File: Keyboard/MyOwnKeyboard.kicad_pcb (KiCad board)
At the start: 2 copper layers, 465 parts, among them J1 Mini-DIN-6, Q1 RFD14N05L, SW1 SW_SPST, SW10 SW_SPST, SW100 SW_SPST, SW101 SW_SPST, SW102 SW_SPST, SW103 SW_SPST, SW104 SW_SPST, SW105 SW_SPST, SW106 SW_SPST, SW107 SW_SPST, SW108 SW_SPST, SW109 SW_SPST, SW11 SW_SPST, SW110 SW_SPST, SW111 SW_SPST, SW112 SW_SPST, SW113 SW_SPST, SW114 SW_SPST, SW12 SW_SPST, SW13 SW_SPST, SW14 SW_SPST, SW15 SW_SPST, SW16 SW_SPST, SW17 SW_SPST, SW18 SW_SPST, SW19 SW_SPST, SW2 SW_SPST, SW20 SW_SPST, SW21 SW_SPST, SW22 SW_SPST, SW23 SW_SPST, SW24 SW_SPST, SW25 SW_SPST, SW26 SW_SPST, SW27 SW_SPST, SW28 SW_SPST, SW29 SW_SPST, SW3 SW_SPST, SW30 SW_SPST, SW31 SW_SPST, SW32 SW_SPST, SW33 SW_SPST, SW34 SW_SPST, SW35 SW_SPST, SW36 SW_SPST, SW37 SW_SPST, SW38 SW_SPST, SW39 SW_SPST, SW4 SW_SPST, SW40 SW_SPST, SW41 SW_SPST, SW42 SW_SPST, SW43 SW_SPST, SW44 SW_SPST, SW45 SW_SPST, SW46 SW_SPST, SW47 SW_SPST, SW48 SW_SPST, SW49 SW_SPST, SW5 SW_SPST, SW50 SW_SPST, SW51 SW_SPST, SW52 SW_SPST, SW53 SW_SPST, SW54 SW_SPST, SW55 SW_SPST, SW56 SW_SPST, SW57 SW_SPST, SW58 SW_SPST, SW59 SW_SPST, SW6 SW_SPST, SW60 SW_SPST, SW61 SW_SPST, SW62 SW_SPST, SW63 SW_SPST, SW64 SW_SPST, SW65 SW_SPST, SW66 SW_SPST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

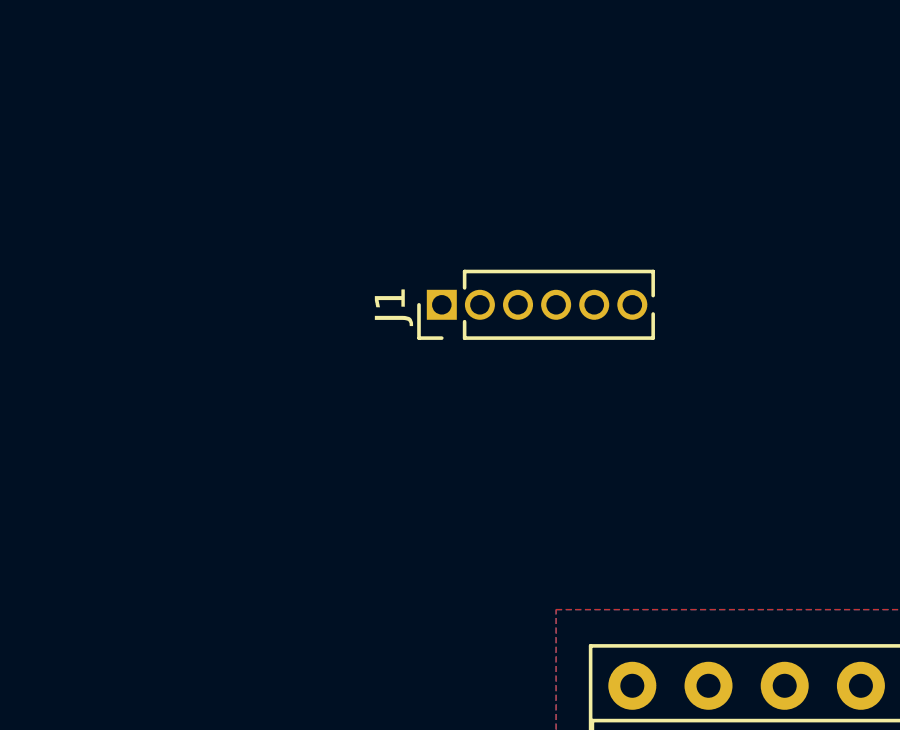
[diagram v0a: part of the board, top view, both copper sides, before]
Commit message: Update keyboard to match changes to keypad
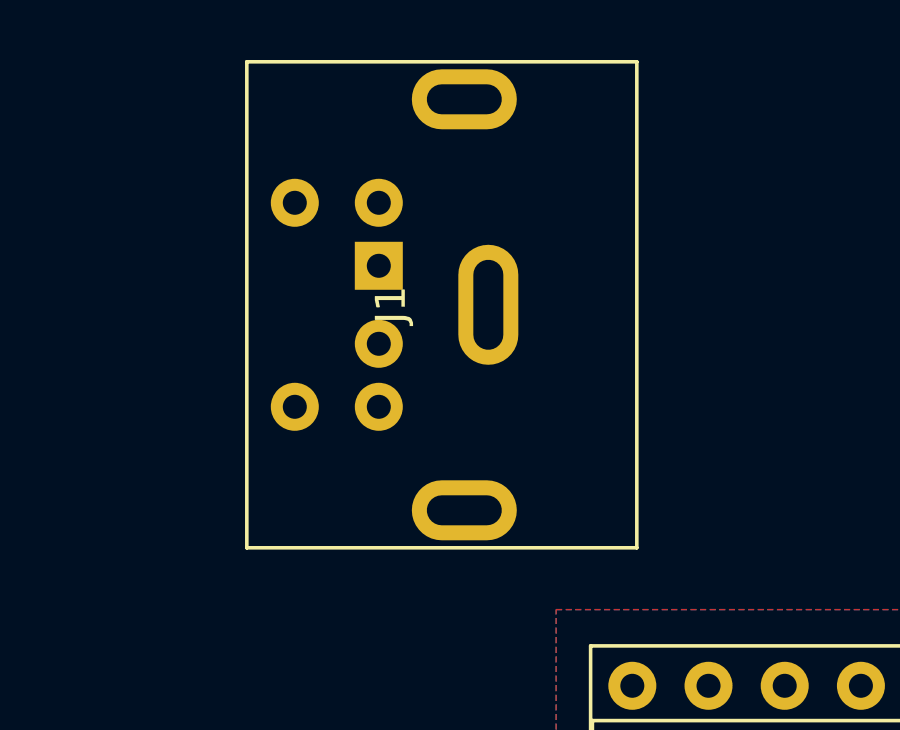
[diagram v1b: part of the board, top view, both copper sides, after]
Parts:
- J1: footprint Connector_PinHeader_1.27mm:PinHeader_1x06_P1.27mm_Vertical -> MyOwnKeyboard:Connector_Mini-DIN_Female_6Pin_2rows
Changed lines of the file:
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@@
     (add_net f)
+  )
+  (module MyOwnKeyboard:Connector_Mini-DIN_Female_6Pin_2rows (layer F.Cu)
+    (at 167.64 39.37 90)
+    (descr "A footprint for the generic 6 pin Mini-DIN through hole connector with shell.")
+    (tags "mini din 6pin connector socket")
+    (fp_text reference J1 (at 0 -1.695 90) (layer F.SilkS)
+      (effects (font (size 1 1) (thickness 0.15)))
+    )
+    (fp_text value Mini-DIN-6 (at 0 8.045 90) (layer F.Fab)
+      (effects (font (size 1 1) (thickness 0.15)))
+    )
+    (fp_line (start 8.49 6.9) (end -8.51 6.9) (layer F.CrtYd) (width 0.05))
+    (fp_line (start 8.49 6.9) (end 8.49 -7.15) (layer F.CrtYd) (width 0.05))
+    (fp_line (start -8.51 -7.15) (end -8.51 6.9) (layer F.CrtYd) (width 0.05))
+    (fp_line (start -8.51 -7.15) (end 8.49 -7.15) (layer F.CrtYd) (width 0.05))
+    (fp_line (start -8.1 6.5) (end 8.1 6.5) (layer F.SilkS) (width 0.12))
+    (fp_line (start -8.1 -6.5) (end 8.1 -6.5) (layer F.SilkS) (width 0.12))
+    (fp_line (start -8.1 -6.5) (end -8.1 6.5) (layer F.SilkS) (width 0.12))
+    (fp_line (start 8.1 -6.5) (end 8.1 6.5) (layer F.SilkS) (width 0.12))
+    (fp_line (start -8 -6.4) (end 8 -6.4) (layer F.Fab) (width 0.1))
+    (fp_line (start -8 6.4) (end -8 -6.4) (layer F.Fab) (width 0.1))
+    (fp_line (start 8 6.4) (end -8 6.4) (layer F.Fab) (width 0.1))
+    (fp_line (start 8 -6.4) (end 8 6.4) (layer F.Fab) (width 0.1))
+    (fp_text user %R (at 0 3.175) (layer F.Fab)
+      (effects (font (size 1 1) (thickness 0.15)))
+    )
+    (pad 7 thru_hole oval (at 0 1.55 90) (size 4 2) (drill oval 3 1) (layers *.Cu *.Mask))
+    (pad 6 thru_hole circle (at -3.4 -4.9 90) (size 1.6 1.6) (drill 0.8) (layers *.Cu *.Mask)
+      (net 268 "Net-(J1-Pad6)"))
+    (pad 5 thru_hole circle (at 3.4 -4.9 90) (size 1.6 1.6) (drill 0.8) (layers *.Cu *.Mask)
+      (net 153 /Clk))
+    (pad 4 thru_hole circle (at -3.4 -2.1 90) (size 1.6 1.6) (drill 0.8) (layers *.Cu *.Mask)
+      (net 141 5v))
+    (pad 3 thru_hole circle (at 3.4 -2.1 90) (size 1.6 1.6) (drill 0.8) (layers *.Cu *.Mask)
+      (net 269 GND))
+    (pad 2 thru_hole circle (at -1.3 -2.1 90) (size 1.6 1.6) (drill 0.8) (layers *.Cu *.Mask)
+      (net 270 "Net-(J1-Pad2)"))
+    (pad 1 thru_hole rect (at 1.3 -2.1 90) (size 1.6 1.6) (drill 0.8) (layers *.Cu *.Mask)
+      (net 151 /Data))
+    (pad 7 thru_hole oval (at 6.85 0.75 90) (size 2 3.5) (drill oval 1 2.5) (layers *.Cu *.Mask))
+    (pad 7 thru_hole oval (at -6.85 0.75 90) (size 2 3.5) (drill oval 1 2.5) (layers *.Cu *.Mask))
   )
   (module Package_DIP:DIP-40_W15.24mm_Socket (layer F.Cu)
@@
       (at (xyz 0 0 0))
       (scale (xyz 1 1 1))
-      (rotate (xyz 0 0 0))
-    )
-  )
-  (module Connector_PinHeader_1.27mm:PinHeader_1x06_P1.27mm_Vertical (layer F.Cu)
-    (at 167.64 39.37 90)
-    (descr "Through hole straight pin header, 1x06, 1.27mm pitch, single row")
-    (tags "Through hole pin header THT 1x06 1.27mm single row")
-    (fp_text reference J1 (at 0 -1.695 90) (layer F.SilkS)
-      (effects (font (size 1 1) (thickness 0.15)))
-    )
-    (fp_text value Mini-DIN-6 (at 0 8.045 90) (layer F.Fab)
-      (effects (font (size 1 1) (thickness 0.15)))
-    )
-    (fp_text user %R (at 0 3.175) (layer F.Fab)
-      (effects (font (size 1 1) (thickness 0.15)))
-    )
-    (fp_line (start 1.55 -1.15) (end -1.55 -1.15) (layer F.CrtYd) (width 0.05))
-    (fp_line (start 1.55 7.5) (end 1.55 -1.15) (layer F.CrtYd) (width 0.05))
-    (fp_line (start -1.55 7.5) (end 1.55 7.5) (layer F.CrtYd) (width 0.05))
-    (fp_line (start -1.55 -1.15) (end -1.55 7.5) (layer F.CrtYd) (width 0.05))
-    (fp_line (start -1.11 -0.76) (end 0 -0.76) (layer F.SilkS) (width 0.12))
-    (fp_line (start -1.11 0) (end -1.11 -0.76) (layer F.SilkS) (width 0.12))
-    (fp_line (start 0.563471 0.76) (end 1.11 0.76) (layer F.SilkS) (width 0.12))
-    (fp_line (start -1.11 0.76) (end -0.563471 0.76) (layer F.SilkS) (width 0.12))
-    (fp_line (start 1.11 0.76) (end 1.11 7.045) (layer F.SilkS) (width 0.12))
-    (fp_line (start -1.11 0.76) (end -1.11 7.045) (layer F.SilkS) (width 0.12))
-    (fp_line (start 0.30753 7.045) (end 1.11 7.045) (layer F.SilkS) (width 0.12))
-    (fp_line (start -1.11 7.045) (end -0.30753 7.045) (layer F.SilkS) (width 0.12))
-    (fp_line (start -1.05 -0.11) (end -0.525 -0.635) (layer F.Fab) (width 0.1))
-    (fp_line (start -1.05 6.985) (end -1.05 -0.11) (layer F.Fab) (width 0.1))
-    (fp_line (start 1.05 6.985) (end -1.05 6.985) (layer F.Fab) (width 0.1))
-    (fp_line (start 1.05 -0.635) (end 1.05 6.985) (layer F.Fab) (width 0.1))
-    (fp_line (start -0.525 -0.635) (end 1.05 -0.635) (layer F.Fab) (width 0.1))
-    (pad 6 thru_hole oval (at 0 6.35 90) (size 1 1) (drill 0.65) (layers *.Cu *.Mask)
-      (net 268 "Net-(J1-Pad6)"))
-    (pad 5 thru_hole oval (at 0 5.08 90) (size 1 1) (drill 0.65) (layers *.Cu *.Mask)
-      (net 153 /Clk))
-    (pad 4 thru_hole oval (at 0 3.81 90) (size 1 1) (drill 0.65) (layers *.Cu *.Mask)
-      (net 141 5v))
-    (pad 3 thru_hole oval (at 0 2.54 90) (size 1 1) (drill 0.65) (layers *.Cu *.Mask)
-      (net 269 GND))
-    (pad 2 thru_hole oval (at 0 1.27 90) (size 1 1) (drill 0.65) (layers *.Cu *.Mask)
-      (net 270 "Net-(J1-Pad2)"))
-    (pad 1 thru_hole rect (at 0 0 90) (size 1 1) (drill 0.65) (layers *.Cu *.Mask)
-      (net 151 /Data))
-    (model ${KISYS3DMOD}/Connector_PinHeader_1.27mm.3dshapes/PinHeader_1x06_P1.27mm_Vertical.wrl
-      (at (xyz 0 0 0))
-      (scale (xyz 1 1 1))

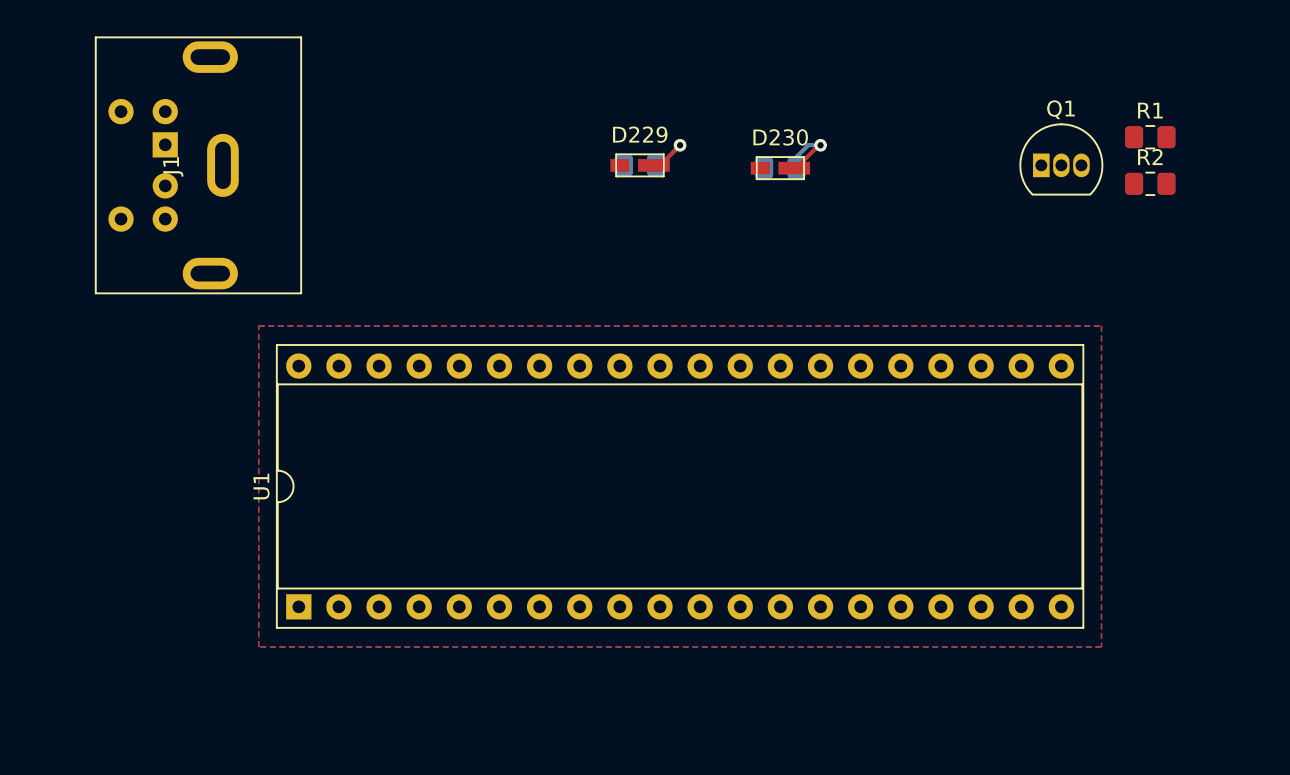
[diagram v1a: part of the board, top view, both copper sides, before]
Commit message: Update keyboard PCB template to match schematic
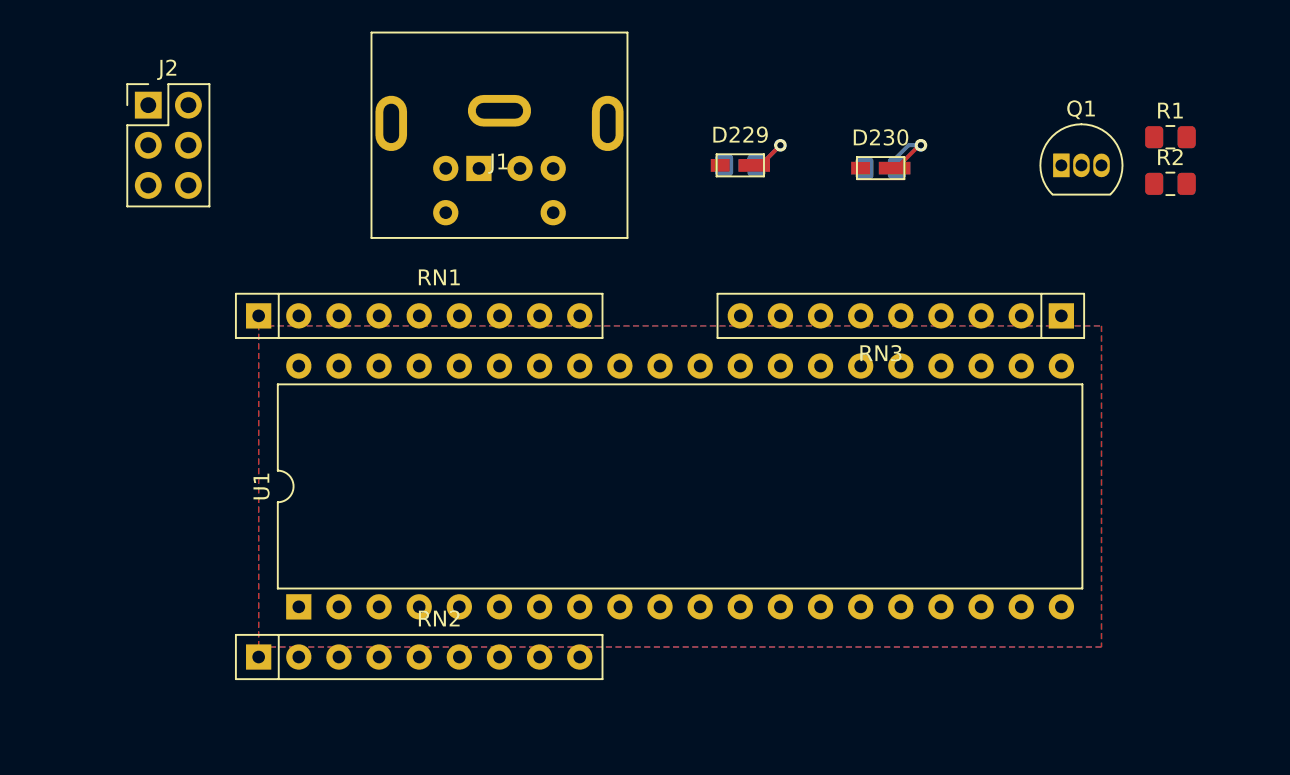
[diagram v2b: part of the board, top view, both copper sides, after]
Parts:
- added J2: ISP Header, Connector_PinHeader_2.54mm:PinHeader_2x03_P2.54mm_Vertical, F.Cu at (164.5, 35.6)
- added RN1: R_Network08, Resistor_THT:R_Array_SIP9, F.Cu at (171.4, 48.9)
- added RN2: R_Network08, Resistor_THT:R_Array_SIP9, F.Cu at (171.4, 70.5)
- added RN3: R_Network08, Resistor_THT:R_Array_SIP9, F.Cu at (222.2, 48.9)
- Q1: value RFD14N05L -> 2N7000
- R10, R100, R101, R102, R103, R104, R105, R106, R107, R108, R109, R11, R110, R111, R112, R113, R114, R115, R116, R117, R118, R12, R13, R14, R15, R16, R17, R18, R19, R20, R21, R22, R23, R24, R25, R26, R27, R28, R29, R3, R30, R31, R32, R33, R34, R35, R36, R37, R38, R39, R4, R40, R41, R42, R43, R44, R45, R46, R47, R48, R49, R5, R50, R51, R52, R53, R54, R55, R56, R57, R58, R59, R6, R60, R61, R62, R63, R64, R65, R66, R67, R68, R69, R7, R70, R71, R72, R73, R74, R75, R76, R77, R78, R79, R8, R80, R81, R82, R83, R84, R85, R86, R87, R88, R89, R9, R90, R91, R92, R93, R94, R95, R96, R97, R98, R99: value 2.3k -> 2.26k
- U1: value ATmega164P-20PU -> ATmega8535-16PU; footprint Package_DIP:DIP-40_W15.24mm_Socket -> Package_DIP:DIP-40_W15.24mm
- moved J1 19.1 mm to (186.7, 37.5), turned to 180 degrees
- moved D229 6.35 mm to (201.9, 39.4)
- moved D230 6.35 mm to (210.8, 39.5)
- moved R117 6.35 mm to (201.9, 39.4)
- moved R118 6.35 mm to (210.8, 39.5)
- moved Q1 1.27 mm to (222.2, 39.4)
- moved R1 1.27 mm to (229.2, 37.6)
- moved R2 1.27 mm to (229.2, 40.5)
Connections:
- net N renamed MOSI
- net O renamed MISO
- net a renamed 1
- net b renamed 2
- net c renamed 3
- net d renamed 4
- net e renamed 5
- net f renamed 6
- J1 pad 3: GND -> Earth
- U1 pad 30: Net-(U1-Pad30) -> 5v
- U1 pad 9: Net-(U1-Pad9) -> RESET

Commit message: Update diode and switch footprints
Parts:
- D1, D10, D100, D101, D102, D103, D104, D105, D106, D107, D108, D109, D11, D110, D111, D112, D113, D114, D12, D13, D14, D15, D16, D17, D18, D19, D2, D20, D21, D22, D23, D24, D25, D26, D27, D28, D29, D3, D30, D31, D32, D33, D34, D35, D36, D37, D38, D39, D4, D40, D41, D42, D43, D44, D45, D46, D47, D48, D49, D5, D50, D51, D52, D53, D54, D55, D56, D57, D58, D59, D6, D60, D61, D62, D63, D64, D65, D66, D67, D68, D69, D7, D70, D71, D72, D73, D74, D75, D76, D77, D78, D79, D8, D80, D81, D82, D83, D84, D85, D86, D87, D88, D89, D9, D90, D91, D92, D93, D94, D95, D96, D97, D98, D99: footprint Diode_THT:D_DO-35_SOD27_P7.62mm_Horizontal -> Diode_SMD:D_MiniMELF_Handsoldering
- SW1, SW10, SW100, SW101, SW102, SW103, SW104, SW105, SW106, SW107, SW108, SW109, SW11, SW110, SW111, SW112, SW113, SW114, SW12, SW13, SW14, SW15, SW16, SW17, SW18, SW19, SW2, SW20, SW21, SW22, SW23, SW24, SW25, SW26, SW27, SW28, SW29, SW3, SW30, SW31, SW32, SW33, SW34, SW35, SW36, SW37, SW38, SW39, SW4, SW40, SW41, SW42, SW43, SW44, SW45, SW46, SW47, SW48, SW49, SW5, SW50, SW51, SW52, SW53, SW54, SW55, SW56, SW57, SW58, SW59, SW6, SW60, SW61, SW62, SW63, SW64, SW65, SW66, SW67, SW68, SW69, SW7, SW70, SW71, SW72, SW73, SW74, SW75, SW76, SW77, SW78, SW79, SW8, SW80, SW81, SW82, SW83, SW84, SW85, SW86, SW87, SW88, SW89, SW9, SW90, SW91, SW92, SW93, SW94, SW95, SW96, SW97, SW98, SW99: footprint MyOwnKeyboard:RomerG -> MyOwnKeyboard:SW_Cherry_MX_1.00u_PCB
- moved D153 4.96 mm to (41.7, 126.9)
- moved D154 4.96 mm to (60.7, 126.9)
- moved D155 4.96 mm to (79.7, 126.9)
- moved D156 4.96 mm to (98.7, 126.9)
- moved D157 4.96 mm to (117.7, 126.9)
- moved D158 4.96 mm to (136.7, 126.9)
- moved D159 4.96 mm to (155.7, 126.9)
- moved D160 4.96 mm to (174.7, 126.9)
- moved D161 4.96 mm to (193.7, 126.9)
- moved D162 4.96 mm to (212.7, 126.9)
- moved D163 4.96 mm to (231.7, 126.9)
- moved D164 4.96 mm to (250.7, 126.9)
- moved D165 4.96 mm to (269.7, 126.9)
- moved D166 4.96 mm to (288.7, 126.9)
- moved D167 4.96 mm to (307.7, 126.9)
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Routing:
- net Net-(D115-Pad1): track 66.8 -> 0.00 mm
- net Net-(D96-Pad2): track 7.86 -> 4.52 mm
- net Net-(D77-Pad2): track 7.86 -> 4.52 mm
- net Net-(D58-Pad2): track 7.86 -> 4.52 mm
- net Net-(D39-Pad2): track 7.86 -> 4.52 mm
- net Net-(D87-Pad2): track 7.86 -> 4.52 mm
- net Net-(D86-Pad2): track 7.86 -> 4.52 mm
- net Net-(D85-Pad2): track 7.86 -> 4.52 mm
- net Net-(D84-Pad2): track 7.86 -> 4.52 mm
- net Net-(D83-Pad2): track 7.86 -> 4.52 mm
- net Net-(D82-Pad2): track 7.86 -> 4.52 mm
- net Net-(D68-Pad2): track 7.86 -> 4.52 mm
- net Net-(D67-Pad2): track 7.86 -> 4.52 mm
- net Net-(D66-Pad2): track 7.86 -> 4.52 mm
- net Net-(D65-Pad2): track 7.86 -> 4.52 mm
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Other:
- net class Power added: clearance 0.2, trace_width 0.5, via_dia 1, via_drill 0.5

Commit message: Reverse diode orientation and reduce pad size
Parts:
- removed RN1, RN2, RN3: R_Network08, Resistor_THT:R_Array_SIP9
- D1, D10, D100, D101, D102, D103, D104, D105, D106, D107, D108, D109, D11, D110, D111, D112, D113, D114, D12, D13, D14, D15, D16, D17, D18, D19, D2, D20, D21, D22, D23, D24, D25, D26, D27, D28, D29, D3, D30, D31, D32, D33, D34, D35, D36, D37, D38, D39, D4, D40, D41, D42, D43, D44, D45, D46, D47, D48, D49, D5, D50, D51, D52, D53, D54, D55, D56, D57, D58, D59, D6, D60, D61, D62, D63, D64, D65, D66, D67, D68, D69, D7, D70, D71, D72, D73, D74, D75, D76, D77, D78, D79, D8, D80, D81, D82, D83, D84, D85, D86, D87, D88, D89, D9, D90, D91, D92, D93, D94, D95, D96, D97, D98, D99: footprint Diode_SMD:D_MiniMELF_Handsoldering -> Diode_SMD:D_MiniMELF
- moved D10 0.80 mm to (220.7, 94.6), turned to 90 degrees
- moved D101 0.80 mm to (144.7, 189.6), turned to 90 degrees
- moved D102 0.80 mm to (163.7, 189.6), turned to 90 degrees
- moved D103 0.80 mm to (182.7, 189.6), turned to 90 degrees
- moved D104 0.80 mm to (201.7, 189.6), turned to 90 degrees
- moved D105 0.80 mm to (220.7, 189.6), turned to 90 degrees
- moved D106 0.80 mm to (239.7, 189.6), turned to 90 degrees
- moved D11 0.80 mm to (239.7, 94.6), turned to 90 degrees
- moved D25 0.80 mm to (144.7, 113.6), turned to 90 degrees
- moved D26 0.80 mm to (163.7, 113.6), turned to 90 degrees
- moved D27 0.80 mm to (182.7, 113.6), turned to 90 degrees
- moved D28 0.80 mm to (201.7, 113.6), turned to 90 degrees
- moved D29 0.80 mm to (220.7, 113.6), turned to 90 degrees
- moved D30 0.80 mm to (239.7, 113.6), turned to 90 degrees
- moved D44 0.80 mm to (144.7, 132.6), turned to 90 degrees
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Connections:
- D1 pad 1: A -> Net-(D1-Pad1)
- D1 pad 2: Net-(D1-Pad2) -> A
- D10 pad 1: J -> Net-(D10-Pad1)
- D10 pad 2: Net-(D10-Pad2) -> J
- D100 pad 1: E -> Net-(D100-Pad1)
- D100 pad 2: Net-(D100-Pad2) -> E
- D101 pad 1: F -> Net-(D101-Pad1)
- D101 pad 2: Net-(D101-Pad2) -> F
- D102 pad 1: G -> Net-(D102-Pad1)
- D102 pad 2: Net-(D102-Pad2) -> G
- D103 pad 1: H -> Net-(D103-Pad1)
- D103 pad 2: Net-(D103-Pad2) -> H
- D104 pad 1: I -> Net-(D104-Pad1)
- D104 pad 2: Net-(D104-Pad2) -> I
- D105 pad 1: J -> Net-(D105-Pad1)
- D105 pad 2: Net-(D105-Pad2) -> J
- D106 pad 1: K -> Net-(D106-Pad1)
- D106 pad 2: Net-(D106-Pad2) -> K
- D107 pad 1: L -> Net-(D107-Pad1)
- D107 pad 2: Net-(D107-Pad2) -> L
- D108 pad 1: M -> Net-(D108-Pad1)
- D108 pad 2: Net-(D108-Pad2) -> M
- D109 pad 1: MOSI -> Net-(D109-Pad1)
- D109 pad 2: Net-(D109-Pad2) -> MOSI
- D11 pad 1: K -> Net-(D11-Pad1)
- D11 pad 2: Net-(D11-Pad2) -> K
- D110 pad 1: MISO -> Net-(D110-Pad1)
- D110 pad 2: Net-(D110-Pad2) -> MISO
- D111 pad 1: P -> Net-(D111-Pad1)
- D111 pad 2: Net-(D111-Pad2) -> P
- D112 pad 1: Q -> Net-(D112-Pad1)
- D112 pad 2: Net-(D112-Pad2) -> Q
- D113 pad 1: R -> Net-(D113-Pad1)
- D113 pad 2: Net-(D113-Pad2) -> R
- D114 pad 1: S -> Net-(D114-Pad1)
- D114 pad 2: Net-(D114-Pad2) -> S
- D12 pad 1: L -> Net-(D12-Pad1)
- D12 pad 2: Net-(D12-Pad2) -> L
- D13 pad 1: M -> Net-(D13-Pad1)
- D13 pad 2: Net-(D13-Pad2) -> M
- D14 pad 1: MOSI -> Net-(D14-Pad1)
- D14 pad 2: Net-(D14-Pad2) -> MOSI
- D15 pad 1: MISO -> Net-(D15-Pad1)
- D15 pad 2: Net-(D15-Pad2) -> MISO
- D16 pad 1: P -> Net-(D16-Pad1)
- D16 pad 2: Net-(D16-Pad2) -> P
- D17 pad 1: Q -> Net-(D17-Pad1)
- D17 pad 2: Net-(D17-Pad2) -> Q
- D18 pad 1: R -> Net-(D18-Pad1)
- D18 pad 2: Net-(D18-Pad2) -> R
- D19 pad 1: S -> Net-(D19-Pad1)
- D19 pad 2: Net-(D19-Pad2) -> S
- D2 pad 1: B -> Net-(D2-Pad1)
- D2 pad 2: Net-(D2-Pad2) -> B
- D20 pad 1: A -> Net-(D20-Pad1)
- D20 pad 2: Net-(D20-Pad2) -> A
- D21 pad 1: B -> Net-(D21-Pad1)
- D21 pad 2: Net-(D21-Pad2) -> B
- D22 pad 1: C -> Net-(D22-Pad1)
- D22 pad 2: Net-(D22-Pad2) -> C
- D23 pad 1: D -> Net-(D23-Pad1)
- D23 pad 2: Net-(D23-Pad2) -> D
- D24 pad 1: E -> Net-(D24-Pad1)
- D24 pad 2: Net-(D24-Pad2) -> E
- D25 pad 1: F -> Net-(D25-Pad1)
- D25 pad 2: Net-(D25-Pad2) -> F
- D26 pad 1: G -> Net-(D26-Pad1)
- D26 pad 2: Net-(D26-Pad2) -> G
- D27 pad 1: H -> Net-(D27-Pad1)
- D27 pad 2: Net-(D27-Pad2) -> H
- D28 pad 1: I -> Net-(D28-Pad1)
- D28 pad 2: Net-(D28-Pad2) -> I
- D29 pad 1: J -> Net-(D29-Pad1)
- D29 pad 2: Net-(D29-Pad2) -> J
- D3 pad 1: C -> Net-(D3-Pad1)
- D3 pad 2: Net-(D3-Pad2) -> C
- D30 pad 1: K -> Net-(D30-Pad1)
- D30 pad 2: Net-(D30-Pad2) -> K
- D31 pad 1: L -> Net-(D31-Pad1)
- D31 pad 2: Net-(D31-Pad2) -> L
- D32 pad 1: M -> Net-(D32-Pad1)
- D32 pad 2: Net-(D32-Pad2) -> M
- D33 pad 1: MOSI -> Net-(D33-Pad1)
- D33 pad 2: Net-(D33-Pad2) -> MOSI
- D34 pad 1: MISO -> Net-(D34-Pad1)
- D34 pad 2: Net-(D34-Pad2) -> MISO
- D35 pad 1: P -> Net-(D35-Pad1)
- D35 pad 2: Net-(D35-Pad2) -> P
- D36 pad 1: Q -> Net-(D36-Pad1)
- D36 pad 2: Net-(D36-Pad2) -> Q
- D37 pad 1: R -> Net-(D37-Pad1)
- D37 pad 2: Net-(D37-Pad2) -> R
- D38 pad 1: S -> Net-(D38-Pad1)
- D38 pad 2: Net-(D38-Pad2) -> S
- D39 pad 1: A -> Net-(D39-Pad1)
- D39 pad 2: Net-(D39-Pad2) -> A
- D4 pad 1: D -> Net-(D4-Pad1)
- D4 pad 2: Net-(D4-Pad2) -> D
- D40 pad 1: B -> Net-(D40-Pad1)
- D40 pad 2: Net-(D40-Pad2) -> B
- D41 pad 1: C -> Net-(D41-Pad1)
- D41 pad 2: Net-(D41-Pad2) -> C
- D42 pad 1: D -> Net-(D42-Pad1)
- D42 pad 2: Net-(D42-Pad2) -> D
- D43 pad 1: E -> Net-(D43-Pad1)
- D43 pad 2: Net-(D43-Pad2) -> E
- D44 pad 1: F -> Net-(D44-Pad1)
- D44 pad 2: Net-(D44-Pad2) -> F
- D45 pad 1: G -> Net-(D45-Pad1)
- D45 pad 2: Net-(D45-Pad2) -> G
- D46 pad 1: H -> Net-(D46-Pad1)
- D46 pad 2: Net-(D46-Pad2) -> H
- D47 pad 1: I -> Net-(D47-Pad1)
- D47 pad 2: Net-(D47-Pad2) -> I
- D48 pad 1: J -> Net-(D48-Pad1)
- D48 pad 2: Net-(D48-Pad2) -> J
- D49 pad 1: K -> Net-(D49-Pad1)
- D49 pad 2: Net-(D49-Pad2) -> K
- D5 pad 1: E -> Net-(D5-Pad1)
- D5 pad 2: Net-(D5-Pad2) -> E
- D50 pad 1: L -> Net-(D50-Pad1)
- D50 pad 2: Net-(D50-Pad2) -> L
- D51 pad 1: M -> Net-(D51-Pad1)
- D51 pad 2: Net-(D51-Pad2) -> M
- D52 pad 1: MOSI -> Net-(D52-Pad1)
- D52 pad 2: Net-(D52-Pad2) -> MOSI
- D53 pad 1: MISO -> Net-(D53-Pad1)
- D53 pad 2: Net-(D53-Pad2) -> MISO
- D54 pad 1: P -> Net-(D54-Pad1)
- D54 pad 2: Net-(D54-Pad2) -> P
- D55 pad 1: Q -> Net-(D55-Pad1)
- D55 pad 2: Net-(D55-Pad2) -> Q
- D56 pad 1: R -> Net-(D56-Pad1)
- D56 pad 2: Net-(D56-Pad2) -> R
- D57 pad 1: S -> Net-(D57-Pad1)
- D57 pad 2: Net-(D57-Pad2) -> S
- D58 pad 1: A -> Net-(D58-Pad1)
- D58 pad 2: Net-(D58-Pad2) -> A
- D59 pad 1: B -> Net-(D59-Pad1)
- D59 pad 2: Net-(D59-Pad2) -> B
- D6 pad 1: F -> Net-(D6-Pad1)
- D6 pad 2: Net-(D6-Pad2) -> F
- D60 pad 1: C -> Net-(D60-Pad1)
- D60 pad 2: Net-(D60-Pad2) -> C
- D61 pad 1: D -> Net-(D61-Pad1)
- D61 pad 2: Net-(D61-Pad2) -> D
- D62 pad 1: E -> Net-(D62-Pad1)
- D62 pad 2: Net-(D62-Pad2) -> E
- D63 pad 1: F -> Net-(D63-Pad1)
- D63 pad 2: Net-(D63-Pad2) -> F
- D64 pad 1: G -> Net-(D64-Pad1)
- D64 pad 2: Net-(D64-Pad2) -> G
- D65 pad 1: H -> Net-(D65-Pad1)
- D65 pad 2: Net-(D65-Pad2) -> H
- D66 pad 1: I -> Net-(D66-Pad1)
- D66 pad 2: Net-(D66-Pad2) -> I
- D67 pad 1: J -> Net-(D67-Pad1)
- D67 pad 2: Net-(D67-Pad2) -> J
- D68 pad 1: K -> Net-(D68-Pad1)
- D68 pad 2: Net-(D68-Pad2) -> K
- D69 pad 1: L -> Net-(D69-Pad1)
- D69 pad 2: Net-(D69-Pad2) -> L
- D7 pad 1: G -> Net-(D7-Pad1)
- D7 pad 2: Net-(D7-Pad2) -> G
- D70 pad 1: M -> Net-(D70-Pad1)
- D70 pad 2: Net-(D70-Pad2) -> M
- D71 pad 1: MOSI -> Net-(D71-Pad1)
- D71 pad 2: Net-(D71-Pad2) -> MOSI
- D72 pad 1: MISO -> Net-(D72-Pad1)
- D72 pad 2: Net-(D72-Pad2) -> MISO
- D73 pad 1: P -> Net-(D73-Pad1)
- D73 pad 2: Net-(D73-Pad2) -> P
- D74 pad 1: Q -> Net-(D74-Pad1)
- D74 pad 2: Net-(D74-Pad2) -> Q
- D75 pad 1: R -> Net-(D75-Pad1)
- D75 pad 2: Net-(D75-Pad2) -> R
- D76 pad 1: S -> Net-(D76-Pad1)
- D76 pad 2: Net-(D76-Pad2) -> S
- D77 pad 1: A -> Net-(D77-Pad1)
- D77 pad 2: Net-(D77-Pad2) -> A
- D78 pad 1: B -> Net-(D78-Pad1)
- D78 pad 2: Net-(D78-Pad2) -> B
- D79 pad 1: C -> Net-(D79-Pad1)
- D79 pad 2: Net-(D79-Pad2) -> C
- D8 pad 1: H -> Net-(D8-Pad1)
- D8 pad 2: Net-(D8-Pad2) -> H
- D80 pad 1: D -> Net-(D80-Pad1)
- D80 pad 2: Net-(D80-Pad2) -> D
- D81 pad 1: E -> Net-(D81-Pad1)
- D81 pad 2: Net-(D81-Pad2) -> E
- D82 pad 1: F -> Net-(D82-Pad1)
- D82 pad 2: Net-(D82-Pad2) -> F
- D83 pad 1: G -> Net-(D83-Pad1)
- D83 pad 2: Net-(D83-Pad2) -> G
- D84 pad 1: H -> Net-(D84-Pad1)
- D84 pad 2: Net-(D84-Pad2) -> H
- D85 pad 1: I -> Net-(D85-Pad1)
- D85 pad 2: Net-(D85-Pad2) -> I
- D86 pad 1: J -> Net-(D86-Pad1)
- D86 pad 2: Net-(D86-Pad2) -> J
- D87 pad 1: K -> Net-(D87-Pad1)
- D87 pad 2: Net-(D87-Pad2) -> K
- D88 pad 1: L -> Net-(D88-Pad1)
- D88 pad 2: Net-(D88-Pad2) -> L
- D89 pad 1: M -> Net-(D89-Pad1)
- D89 pad 2: Net-(D89-Pad2) -> M
- D9 pad 1: I -> Net-(D9-Pad1)
- D9 pad 2: Net-(D9-Pad2) -> I
- D90 pad 1: MOSI -> Net-(D90-Pad1)
- D90 pad 2: Net-(D90-Pad2) -> MOSI
- D91 pad 1: MISO -> Net-(D91-Pad1)
- D91 pad 2: Net-(D91-Pad2) -> MISO
- D92 pad 1: P -> Net-(D92-Pad1)
- D92 pad 2: Net-(D92-Pad2) -> P
- D93 pad 1: Q -> Net-(D93-Pad1)
- D93 pad 2: Net-(D93-Pad2) -> Q
- D94 pad 1: R -> Net-(D94-Pad1)
- D94 pad 2: Net-(D94-Pad2) -> R
- D95 pad 1: S -> Net-(D95-Pad1)
- D95 pad 2: Net-(D95-Pad2) -> S
- D96 pad 1: A -> Net-(D96-Pad1)
- D96 pad 2: Net-(D96-Pad2) -> A
- D97 pad 1: B -> Net-(D97-Pad1)
- D97 pad 2: Net-(D97-Pad2) -> B
- D98 pad 1: C -> Net-(D98-Pad1)
- D98 pad 2: Net-(D98-Pad2) -> C
- D99 pad 1: D -> Net-(D99-Pad1)
- D99 pad 2: Net-(D99-Pad2) -> D
- SW1 pad 2: Net-(D1-Pad2) -> Net-(D1-Pad1)
- SW10 pad 2: Net-(D10-Pad2) -> Net-(D10-Pad1)
- SW100 pad 2: Net-(D100-Pad2) -> Net-(D100-Pad1)
- SW101 pad 2: Net-(D101-Pad2) -> Net-(D101-Pad1)
- SW102 pad 2: Net-(D102-Pad2) -> Net-(D102-Pad1)
- SW103 pad 2: Net-(D103-Pad2) -> Net-(D103-Pad1)
- SW104 pad 2: Net-(D104-Pad2) -> Net-(D104-Pad1)
- SW105 pad 2: Net-(D105-Pad2) -> Net-(D105-Pad1)
- SW106 pad 2: Net-(D106-Pad2) -> Net-(D106-Pad1)
- SW107 pad 2: Net-(D107-Pad2) -> Net-(D107-Pad1)
- SW108 pad 2: Net-(D108-Pad2) -> Net-(D108-Pad1)
- SW109 pad 2: Net-(D109-Pad2) -> Net-(D109-Pad1)
- SW11 pad 2: Net-(D11-Pad2) -> Net-(D11-Pad1)
- SW110 pad 2: Net-(D110-Pad2) -> Net-(D110-Pad1)
- SW111 pad 2: Net-(D111-Pad2) -> Net-(D111-Pad1)
- SW112 pad 2: Net-(D112-Pad2) -> Net-(D112-Pad1)
- SW113 pad 2: Net-(D113-Pad2) -> Net-(D113-Pad1)
- SW114 pad 2: Net-(D114-Pad2) -> Net-(D114-Pad1)
- SW12 pad 2: Net-(D12-Pad2) -> Net-(D12-Pad1)
- SW13 pad 2: Net-(D13-Pad2) -> Net-(D13-Pad1)
- SW14 pad 2: Net-(D14-Pad2) -> Net-(D14-Pad1)
- SW15 pad 2: Net-(D15-Pad2) -> Net-(D15-Pad1)
- SW16 pad 2: Net-(D16-Pad2) -> Net-(D16-Pad1)
- SW17 pad 2: Net-(D17-Pad2) -> Net-(D17-Pad1)
- SW18 pad 2: Net-(D18-Pad2) -> Net-(D18-Pad1)
- SW19 pad 2: Net-(D19-Pad2) -> Net-(D19-Pad1)
- SW2 pad 2: Net-(D2-Pad2) -> Net-(D2-Pad1)
- SW20 pad 2: Net-(D20-Pad2) -> Net-(D20-Pad1)
- SW21 pad 2: Net-(D21-Pad2) -> Net-(D21-Pad1)
- SW22 pad 2: Net-(D22-Pad2) -> Net-(D22-Pad1)
- SW23 pad 2: Net-(D23-Pad2) -> Net-(D23-Pad1)
- SW24 pad 2: Net-(D24-Pad2) -> Net-(D24-Pad1)
- SW25 pad 2: Net-(D25-Pad2) -> Net-(D25-Pad1)
- SW26 pad 2: Net-(D26-Pad2) -> Net-(D26-Pad1)
- SW27 pad 2: Net-(D27-Pad2) -> Net-(D27-Pad1)
- SW28 pad 2: Net-(D28-Pad2) -> Net-(D28-Pad1)
- SW29 pad 2: Net-(D29-Pad2) -> Net-(D29-Pad1)
- SW3 pad 2: Net-(D3-Pad2) -> Net-(D3-Pad1)
- SW30 pad 2: Net-(D30-Pad2) -> Net-(D30-Pad1)
- SW31 pad 2: Net-(D31-Pad2) -> Net-(D31-Pad1)
- SW32 pad 2: Net-(D32-Pad2) -> Net-(D32-Pad1)
- SW33 pad 2: Net-(D33-Pad2) -> Net-(D33-Pad1)
- SW34 pad 2: Net-(D34-Pad2) -> Net-(D34-Pad1)
- SW35 pad 2: Net-(D35-Pad2) -> Net-(D35-Pad1)
- SW36 pad 2: Net-(D36-Pad2) -> Net-(D36-Pad1)
- SW37 pad 2: Net-(D37-Pad2) -> Net-(D37-Pad1)
- SW38 pad 2: Net-(D38-Pad2) -> Net-(D38-Pad1)
- SW39 pad 2: Net-(D39-Pad2) -> Net-(D39-Pad1)
- SW4 pad 2: Net-(D4-Pad2) -> Net-(D4-Pad1)
- SW40 pad 2: Net-(D40-Pad2) -> Net-(D40-Pad1)
- SW41 pad 2: Net-(D41-Pad2) -> Net-(D41-Pad1)
- SW42 pad 2: Net-(D42-Pad2) -> Net-(D42-Pad1)
- SW43 pad 2: Net-(D43-Pad2) -> Net-(D43-Pad1)
- SW44 pad 2: Net-(D44-Pad2) -> Net-(D44-Pad1)
- SW45 pad 2: Net-(D45-Pad2) -> Net-(D45-Pad1)
- SW46 pad 2: Net-(D46-Pad2) -> Net-(D46-Pad1)
- SW47 pad 2: Net-(D47-Pad2) -> Net-(D47-Pad1)
- SW48 pad 2: Net-(D48-Pad2) -> Net-(D48-Pad1)
- SW49 pad 2: Net-(D49-Pad2) -> Net-(D49-Pad1)
- SW5 pad 2: Net-(D5-Pad2) -> Net-(D5-Pad1)
- SW50 pad 2: Net-(D50-Pad2) -> Net-(D50-Pad1)
- SW51 pad 2: Net-(D51-Pad2) -> Net-(D51-Pad1)
- SW52 pad 2: Net-(D52-Pad2) -> Net-(D52-Pad1)
- SW53 pad 2: Net-(D53-Pad2) -> Net-(D53-Pad1)
- SW54 pad 2: Net-(D54-Pad2) -> Net-(D54-Pad1)
- SW55 pad 2: Net-(D55-Pad2) -> Net-(D55-Pad1)
- SW56 pad 2: Net-(D56-Pad2) -> Net-(D56-Pad1)
- SW57 pad 2: Net-(D57-Pad2) -> Net-(D57-Pad1)
- SW58 pad 2: Net-(D58-Pad2) -> Net-(D58-Pad1)
- SW59 pad 2: Net-(D59-Pad2) -> Net-(D59-Pad1)
- SW6 pad 2: Net-(D6-Pad2) -> Net-(D6-Pad1)
- SW60 pad 2: Net-(D60-Pad2) -> Net-(D60-Pad1)
- SW61 pad 2: Net-(D61-Pad2) -> Net-(D61-Pad1)
- SW62 pad 2: Net-(D62-Pad2) -> Net-(D62-Pad1)
- SW63 pad 2: Net-(D63-Pad2) -> Net-(D63-Pad1)
- SW64 pad 2: Net-(D64-Pad2) -> Net-(D64-Pad1)
- SW65 pad 2: Net-(D65-Pad2) -> Net-(D65-Pad1)
- SW66 pad 2: Net-(D66-Pad2) -> Net-(D66-Pad1)
- SW67 pad 2: Net-(D67-Pad2) -> Net-(D67-Pad1)
- SW68 pad 2: Net-(D68-Pad2) -> Net-(D68-Pad1)
- SW69 pad 2: Net-(D69-Pad2) -> Net-(D69-Pad1)
- SW7 pad 2: Net-(D7-Pad2) -> Net-(D7-Pad1)
- SW70 pad 2: Net-(D70-Pad2) -> Net-(D70-Pad1)
- SW71 pad 2: Net-(D71-Pad2) -> Net-(D71-Pad1)
- SW72 pad 2: Net-(D72-Pad2) -> Net-(D72-Pad1)
- SW73 pad 2: Net-(D73-Pad2) -> Net-(D73-Pad1)
- SW74 pad 2: Net-(D74-Pad2) -> Net-(D74-Pad1)
- SW75 pad 2: Net-(D75-Pad2) -> Net-(D75-Pad1)
- SW76 pad 2: Net-(D76-Pad2) -> Net-(D76-Pad1)
- SW77 pad 2: Net-(D77-Pad2) -> Net-(D77-Pad1)
- SW78 pad 2: Net-(D78-Pad2) -> Net-(D78-Pad1)
- SW79 pad 2: Net-(D79-Pad2) -> Net-(D79-Pad1)
- SW8 pad 2: Net-(D8-Pad2) -> Net-(D8-Pad1)
- SW80 pad 2: Net-(D80-Pad2) -> Net-(D80-Pad1)
- SW81 pad 2: Net-(D81-Pad2) -> Net-(D81-Pad1)
- SW82 pad 2: Net-(D82-Pad2) -> Net-(D82-Pad1)
- SW83 pad 2: Net-(D83-Pad2) -> Net-(D83-Pad1)
- SW84 pad 2: Net-(D84-Pad2) -> Net-(D84-Pad1)
- SW85 pad 2: Net-(D85-Pad2) -> Net-(D85-Pad1)
- SW86 pad 2: Net-(D86-Pad2) -> Net-(D86-Pad1)
- SW87 pad 2: Net-(D87-Pad2) -> Net-(D87-Pad1)
- SW88 pad 2: Net-(D88-Pad2) -> Net-(D88-Pad1)
- SW89 pad 2: Net-(D89-Pad2) -> Net-(D89-Pad1)
- SW9 pad 2: Net-(D9-Pad2) -> Net-(D9-Pad1)
- SW90 pad 2: Net-(D90-Pad2) -> Net-(D90-Pad1)
- SW91 pad 2: Net-(D91-Pad2) -> Net-(D91-Pad1)
- SW92 pad 2: Net-(D92-Pad2) -> Net-(D92-Pad1)
- SW93 pad 2: Net-(D93-Pad2) -> Net-(D93-Pad1)
- SW94 pad 2: Net-(D94-Pad2) -> Net-(D94-Pad1)
- SW95 pad 2: Net-(D95-Pad2) -> Net-(D95-Pad1)
- SW96 pad 2: Net-(D96-Pad2) -> Net-(D96-Pad1)
- SW97 pad 2: Net-(D97-Pad2) -> Net-(D97-Pad1)
- SW98 pad 2: Net-(D98-Pad2) -> Net-(D98-Pad1)
- SW99 pad 2: Net-(D99-Pad2) -> Net-(D99-Pad1)
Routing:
- net Net-(D1-Pad1): track 0.00 -> 8.39 mm
- net Net-(D95-Pad2): track 4.52 -> 0.00 mm
- net Net-(D94-Pad2): track 4.52 -> 0.00 mm
- net Net-(D93-Pad2): track 4.52 -> 0.00 mm
- net Net-(D92-Pad2): track 4.52 -> 0.00 mm
- net Net-(D91-Pad2): track 4.52 -> 0.00 mm
- net Net-(D90-Pad2): track 4.52 -> 0.00 mm
- net Net-(D89-Pad2): track 4.52 -> 0.00 mm
- net Net-(D76-Pad2): track 4.52 -> 0.00 mm
- net Net-(D75-Pad2): track 4.52 -> 0.00 mm
- net Net-(D74-Pad2): track 4.52 -> 0.00 mm
- net Net-(D73-Pad2): track 4.52 -> 0.00 mm
- net Net-(D72-Pad2): track 4.52 -> 0.00 mm
- net Net-(D71-Pad2): track 4.52 -> 0.00 mm
- net Net-(D70-Pad2): track 4.52 -> 0.00 mm
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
